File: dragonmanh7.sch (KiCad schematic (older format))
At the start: 110 parts, among them J1 USB_B, J10 Conn_02x12_Odd_Even, J11 Conn_02x03_Odd_Even, J12 VBAT+, J13 Conn_02x05_Odd_Even, J14 VBATG, J15 Conn_02x02_Odd_Even, J18 Conn_02x05_Odd_Even, J2 73725-0110BLF, J3 RJ45_Amphenol_RJMG1BD3B8K1ANR, J4 Micro_SD_Card, J5 Screw_Terminal_01x06, J6 Conn_02x12_Odd_Even, J7 USB_B, J8 Screw_Terminal_01x02, J9 Conn_02x12_Odd_Even, SW1 RESET, SW2 PC13, U1 STM32H743VITx, U10 USBLC6-2SC6, U12 TCAN332, U13 ISL83483, U14 MIC2005A, U2 KSZ8081RNA, U5 S25FL127SABMFI101, U6 AP63203, U7 USBLC6-2SC6, U8 STM32F042F6Px, U9 USBLC6-2SC6, Y1 8MHz, Y2 32.768KHz, Y3 25MHz

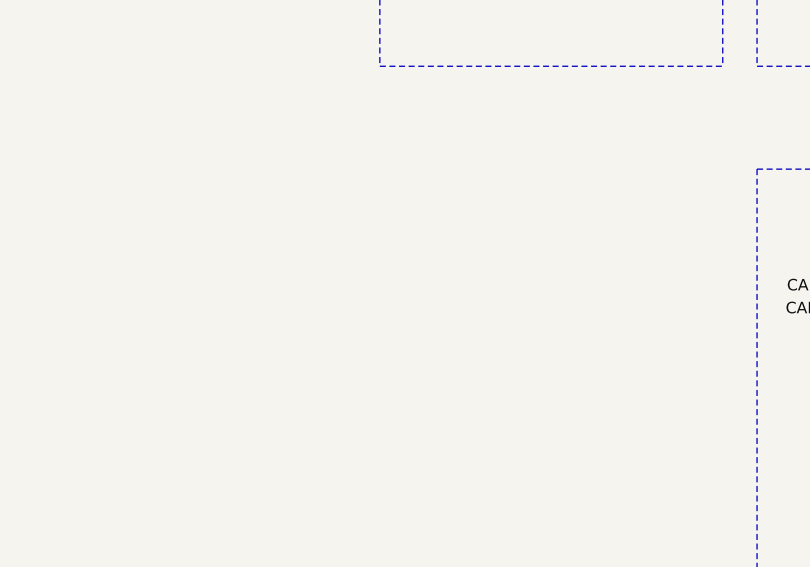
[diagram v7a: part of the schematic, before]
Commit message: Add fidutial for automatic mounting
Signed-off-by: Martin Ribelotta <martinribelotta@gmail.com>
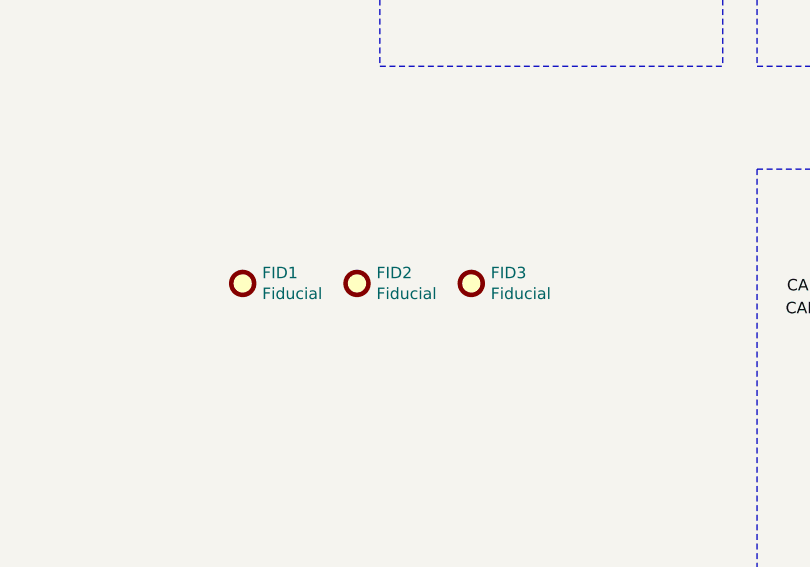
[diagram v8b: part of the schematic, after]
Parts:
- added FID1, FID2, FID3: Fiducial, Fiducial:Fiducial_1mm_Mask2mm, symbol Mechanical:Fiducial
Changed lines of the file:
@@
 Wire Wire Line
 	13950 4000 14000 4000
+$Comp
+L Mechanical:Fiducial FID1
+U 1 1 5E22DD76
+P 10050 3850
+F 0 "FID1" H 10135 3896 50  0000 L CNN
+F 1 "Fiducial" H 10135 3805 50  0000 L CNN
+F 2 "Fiducial:Fiducial_1mm_Mask2mm" H 10050 3850 50  0001 C CNN
+F 3 "~" H 10050 3850 50  0001 C CNN
+	1    10050 3850
+	1    0    0    -1
+$EndComp
+$Comp
+L Mechanical:Fiducial FID2
+U 1 1 5E22E743
+P 10550 3850
+F 0 "FID2" H 10635 3896 50  0000 L CNN
+F 1 "Fiducial" H 10635 3805 50  0000 L CNN
+F 2 "Fiducial:Fiducial_1mm_Mask2mm" H 10550 3850 50  0001 C CNN
+F 3 "~" H 10550 3850 50  0001 C CNN
+	1    10550 3850
+	1    0    0    -1
+$EndComp
+$Comp
+L Mechanical:Fiducial FID3
+U 1 1 5E22EA10
+P 11050 3850
+F 0 "FID3" H 11135 3896 50  0000 L CNN
+F 1 "Fiducial" H 11135 3805 50  0000 L CNN
+F 2 "Fiducial:Fiducial_1mm_Mask2mm" H 11050 3850 50  0001 C CNN
+F 3 "~" H 11050 3850 50  0001 C CNN
+	1    11050 3850
+	1    0    0    -1
+$EndComp
 $EndSCHEMATC
